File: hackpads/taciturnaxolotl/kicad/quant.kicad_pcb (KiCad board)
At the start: 2 copper layers, 59.4 x 82 mm, 16 parts, among them SW1 SW_Push, SW2 SW_Push, SW3 SW_Push, SW4 SW_Push, SW5 SW_Push, SW6 SW_Push, SW7 SW_Push, SW8 SW_Push, SW9 SW_Push, U1 XIAO-RP2040-DIP

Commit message: chore: fix drc
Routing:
- net +5V: track 76.3 -> 80.9 mm
- net Net-(D1-DOUT): track 9.14 -> 10.4 mm

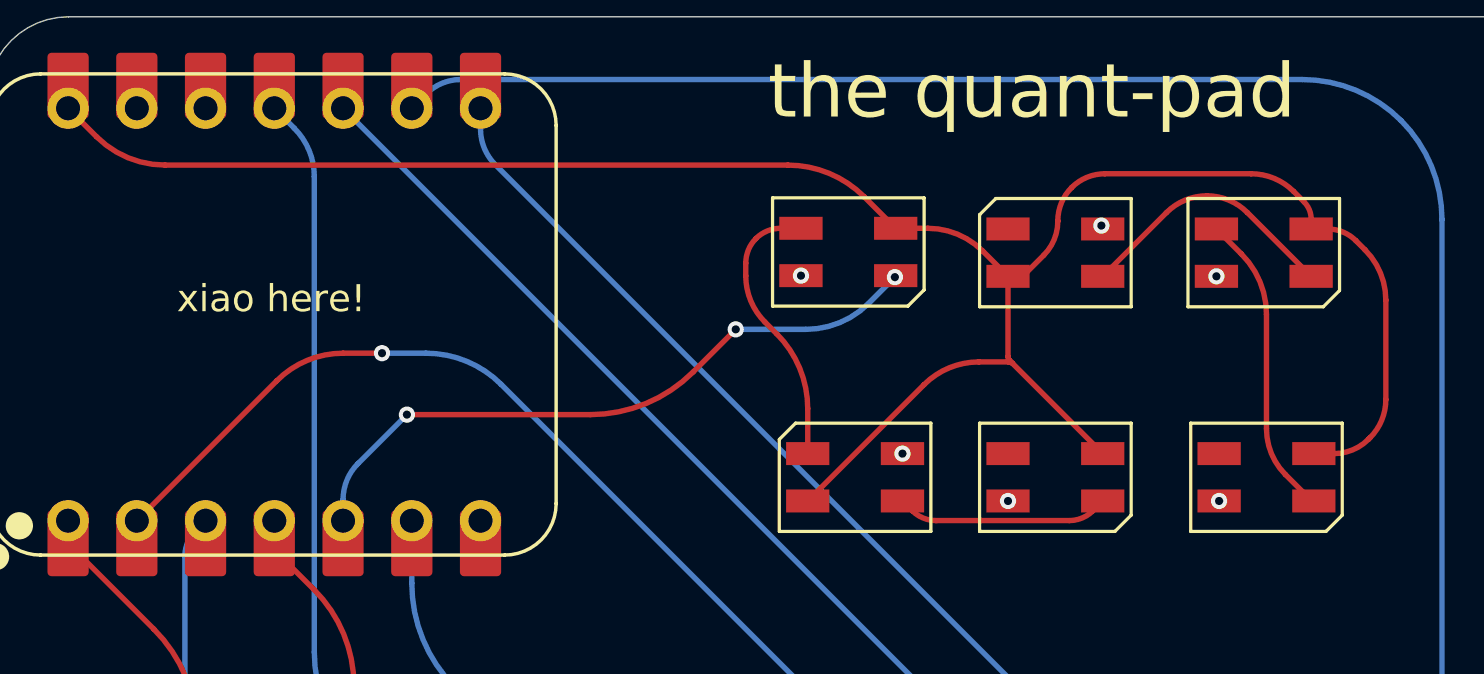
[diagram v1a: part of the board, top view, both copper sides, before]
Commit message: chore: move vias off pads
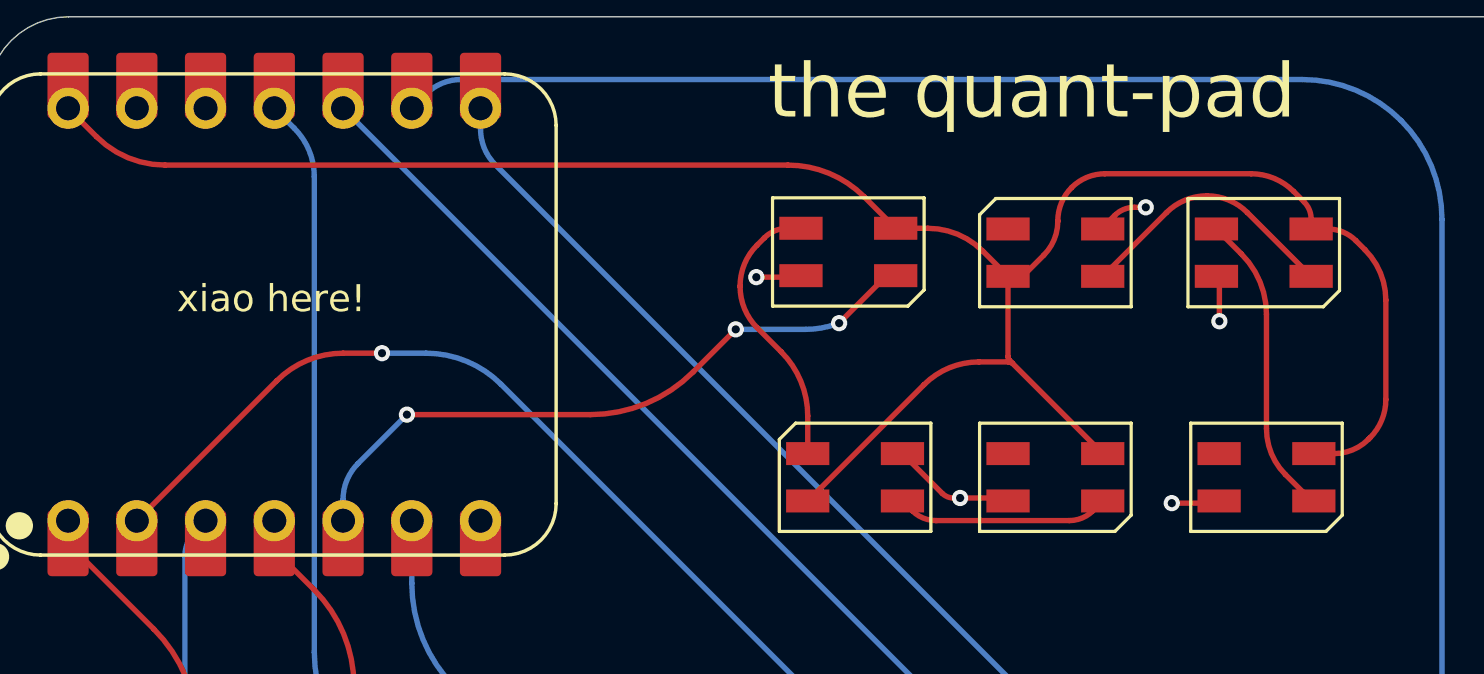
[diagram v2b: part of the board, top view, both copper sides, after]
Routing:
- net GND: track 0.14 -> 11.6 mm, vias 6 -> 5
